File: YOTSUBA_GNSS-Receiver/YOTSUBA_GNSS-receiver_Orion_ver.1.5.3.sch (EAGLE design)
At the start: 49 parts, among them IC2 NJM12877F33-TE1, J1 USB4500-03-0-A_REVA, J2 DF37B-10DP-0.4V_53_, U1 CP2102N-A01-GQFN28, U2 SF1186B-2, U3 MAX2670GTB+T

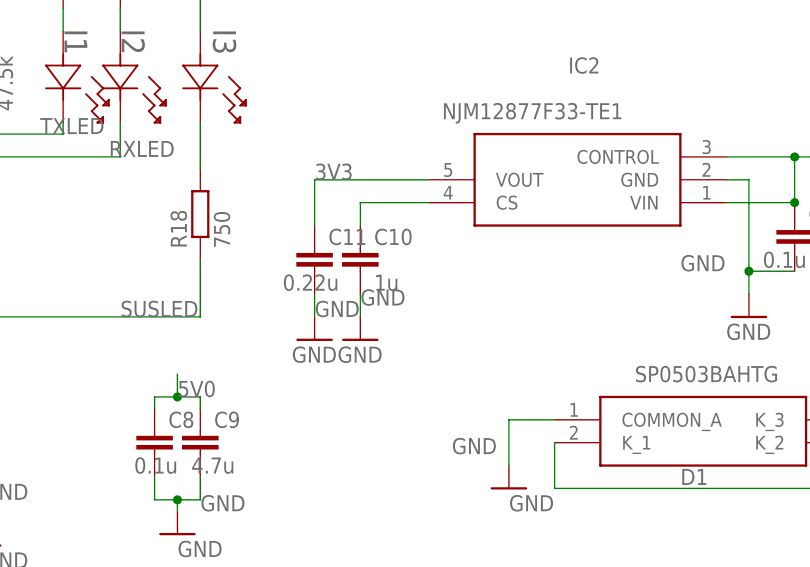
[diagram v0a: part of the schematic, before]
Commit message: C10 modified
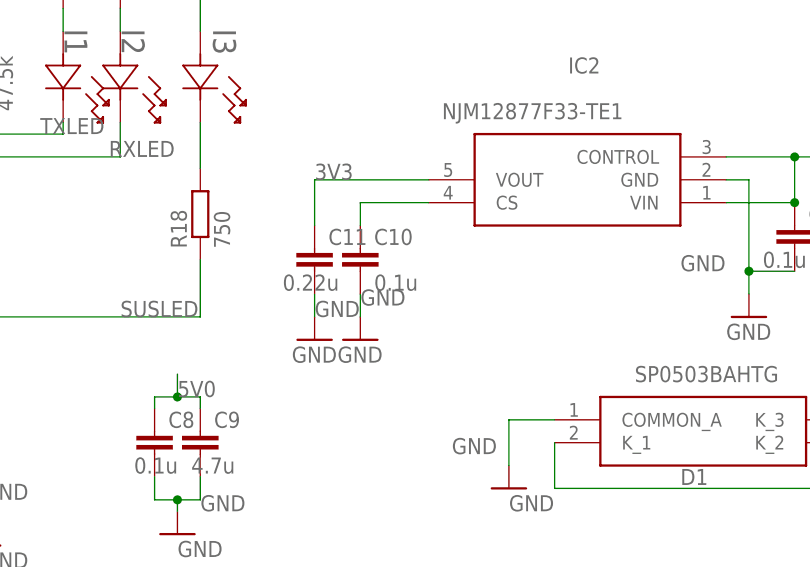
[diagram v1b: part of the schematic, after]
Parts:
- C10: value 1u -> 0.1u
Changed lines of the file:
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@@
 <part name="GND21" library="supply1" library_urn="urn:adsk.eagle:library:371" deviceset="GND" device=""/>
 <part name="IC2" library="SamacSys_Parts" library_urn="urn:adsk.eagle:library:38878568" deviceset="NJM12877F33-TE1" device="" package3d_urn="urn:adsk.eagle:package:38878576/2"/>
-<part name="C10" library="rcl" deviceset="C-EU" device="C1608" package3d_urn="urn:adsk.eagle:package:23621/2" value="1u"/>
+<part name="C10" library="rcl" deviceset="C-EU" device="C1608" package3d_urn="urn:adsk.eagle:package:23621/2" value="0.1u"/>
 <part name="GND22" library="supply1" library_urn="urn:adsk.eagle:library:371" deviceset="GND" device=""/>
 <part name="C11" library="rcl" deviceset="C-EU" device="C1608" package3d_urn="urn:adsk.eagle:package:23621/2" value="0.22u"/>
